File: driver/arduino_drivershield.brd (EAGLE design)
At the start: 60 x 53.7 mm, 37 parts, among them IC1 LB1973M, IC10 LB1973M, IC11 LB1973M, IC12 74HC14D, IC2 LB1973M, IC3 74HC14D, IC4 LB1973M, IC5 LB1973M, IC6 74HC14D, IC7 LB1973M, IC8 LB1973M, IC9 74HC14D, U1 ARDUINO_SHIELDLABEL

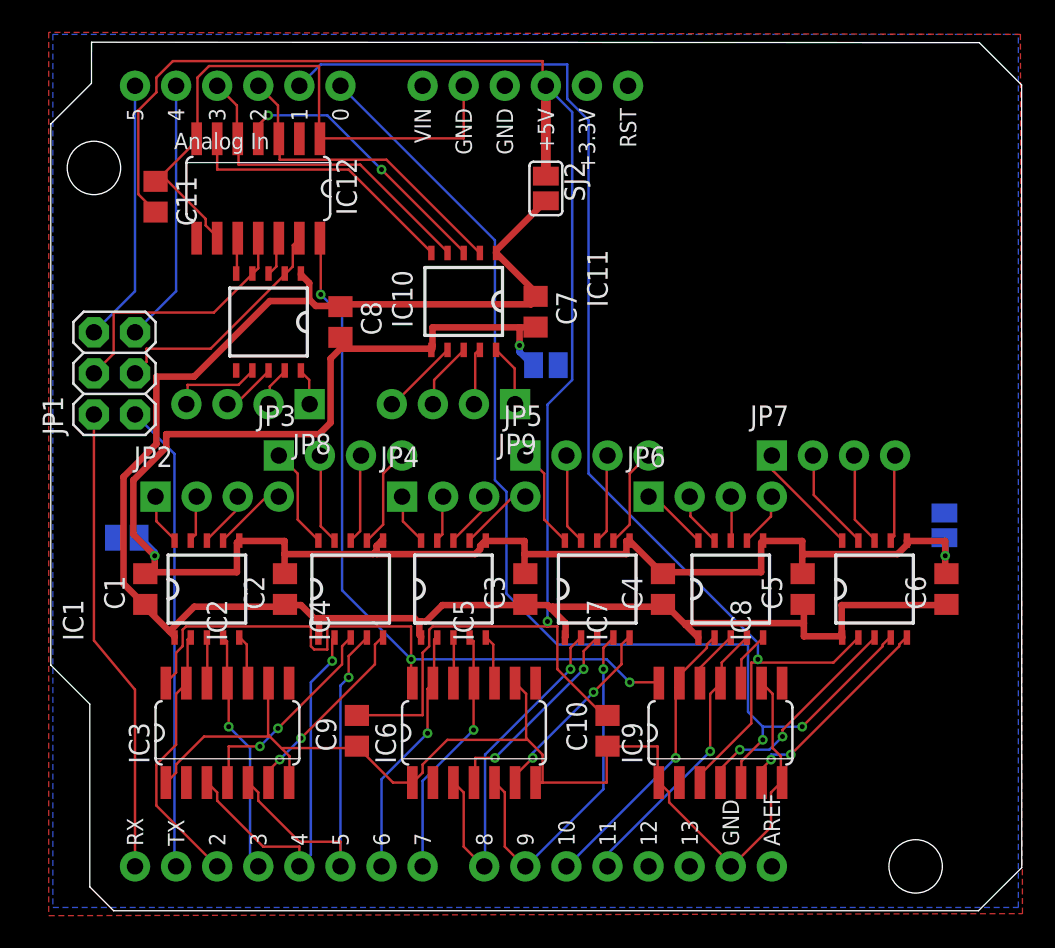
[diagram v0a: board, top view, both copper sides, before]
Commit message: crap, there was still a leftover from myh signal namig adventures
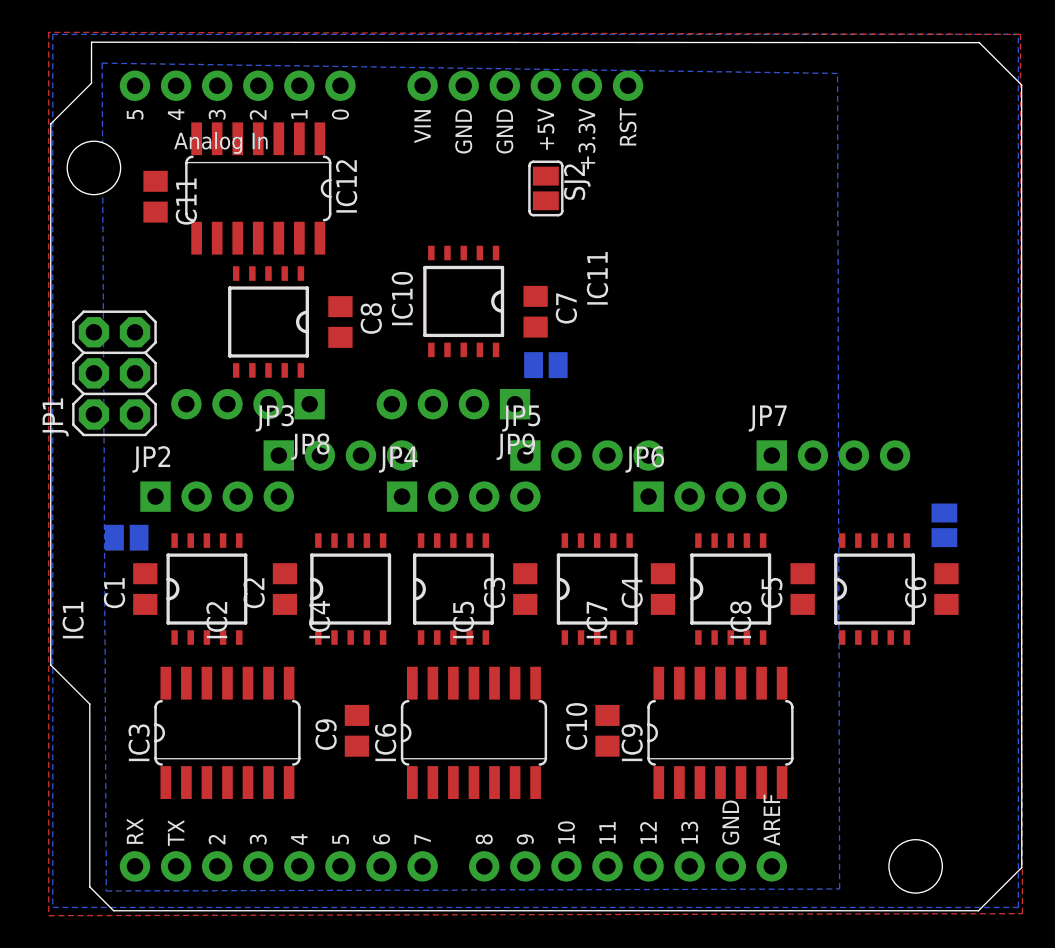
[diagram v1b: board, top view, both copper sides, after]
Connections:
- removed net 5V@1: IC12.14, IC3.14, IC6.14, IC9.14
- net 5V: now also IC12.14, IC3.14, IC6.14, IC9.14
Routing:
- net V+: track 114.7 -> 0.00 mm
- net FOO: track 110.5 -> 0.00 mm, vias 3 -> 0
- net GND: track 109.3 -> 0.00 mm
- net 5V: track 99.9 -> 0.00 mm, vias 1 -> 0
- net N$28: track 75.0 -> 0.00 mm, vias 1 -> 0
- net N$51: track 71.6 -> 0.00 mm, vias 2 -> 0
- net 5V@1: track 68.4 -> 0.00 mm, vias 3 -> 0
- net TX: track 29.0 -> 0.00 mm
- net RX: track 28.9 -> 0.00 mm
- net N$15: track 23.9 -> 0.00 mm, vias 1 -> 0
- net N$16: track 23.9 -> 0.00 mm, vias 1 -> 0
- net N$35: track 22.7 -> 0.00 mm, vias 1 -> 0
- net N$36: track 22.4 -> 0.00 mm, vias 1 -> 0
- net N$66: track 20.6 -> 0.00 mm
- net N$30: track 19.9 -> 0.00 mm
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- added copper zone on layer 16, net N$31

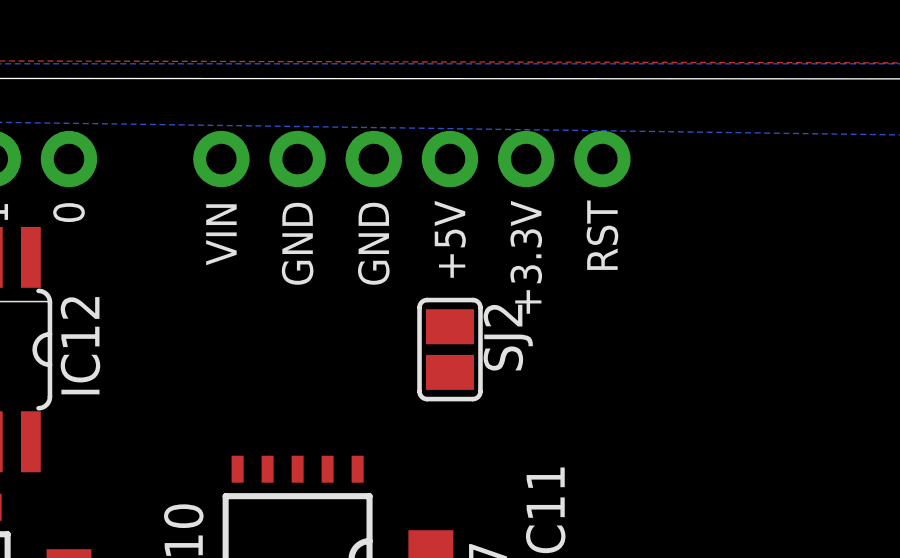
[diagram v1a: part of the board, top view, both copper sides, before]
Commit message: maybe now all my old follies are fixed?
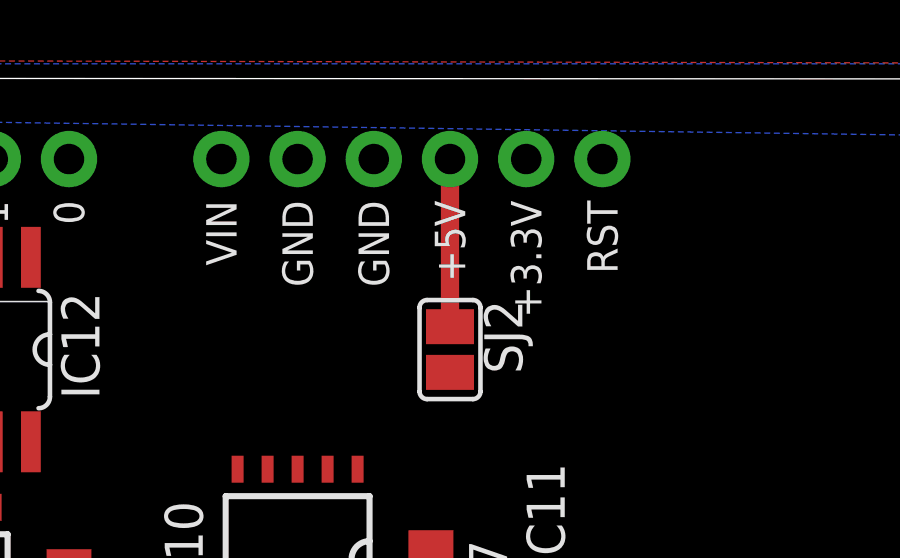
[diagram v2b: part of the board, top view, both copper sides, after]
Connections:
- net FOO: no longer SJ1.1
- net GND@PWR: now also SJ1.1
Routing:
- net 5V: track 0.00 -> 5.59 mm
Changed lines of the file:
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@@
 <contactref element="IC11" pad="6"/>
 <contactref element="IC11" pad="6"/>
-<contactref element="SJ1" pad="1"/>
 <contactref element="SJ3" pad="1"/>
 <contactref element="SJ4" pad="1"/>
@@
 <wire x1="5.715" y1="20.635" x2="11.525" y2="22.681" width="0" layer="19" extent="1-1"/>
 <wire x1="5.334" y1="22.86" x2="5.715" y2="20.635" width="0" layer="19" extent="1-16"/>
-<wire x1="29.718" y1="33.528" x2="26.765" y2="22.681" width="0" layer="19" extent="1-16"/>
-<wire x1="29.845" y1="35.88" x2="29.718" y2="33.528" width="0" layer="19" extent="1-16"/>
-<wire x1="23.4" y1="34.469" x2="29.718" y2="33.528" width="0" layer="19" extent="1-16"/>
+<wire x1="23.4" y1="34.469" x2="20.415" y2="22.681" width="0" layer="19" extent="1-1"/>
 <wire x1="17.78" y1="35.245" x2="23.4" y2="34.469" width="0" layer="19" extent="1-1"/>
+<wire x1="29.845" y1="35.88" x2="23.4" y2="34.469" width="0" layer="19" extent="1-1"/>
 </signal>
 <signal name="GND">
@@
 <contactref element="IC9" pad="14"/>
 <contactref element="IC12" pad="14"/>
-<wire x1="30.48" y1="45.212" x2="30.48" y2="50.8" width="0" layer="19" extent="1-1"/>
+<wire x1="30.48" y1="45.212" x2="30.48" y2="50.8" width="0.6096" layer="1"/>
 <wire x1="16.51" y1="41.3766" x2="30.48" y2="45.212" width="0" layer="19" extent="1-1"/>
 <wire x1="6.35" y1="42.992" x2="16.51" y2="41.3766" width="0" layer="19" extent="1-1"/>
@@
 <signal name="GND@PWR" class="1">
 <contactref element="IC10" pad="6"/>
+<contactref element="SJ1" pad="1"/>
+<wire x1="11.335" y1="33.199" x2="29.718" y2="33.528" width="0" layer="19" extent="1-16"/>
 </signal>
 <signal name="N$31">

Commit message: maybe now all my old follies are fixed?
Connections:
- removed net FOO: C1.2, C2.2, C3.2, C4.2, C5.2, C6.2, C7.2, C8.2, IC1.6, IC11.6, IC2.6, IC4.6, IC5.6, IC7.6, IC8.6, SJ3.1, SJ4.1
- net GND@PWR: now also C1.2, C2.2, C3.2, C4.2, C5.2, C6.2, C7.2, C8.2, IC1.6, IC11.6, IC2.6, IC4.6, IC5.6, IC7.6, IC8.6, SJ3.1, SJ4.1
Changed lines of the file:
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@@
 <wire x1="5.715" y1="18.735" x2="7.525" y2="16.689" width="0" layer="19" extent="1-1"/>
-</signal>
-<signal name="FOO" class="1">
-<contactref element="IC8" pad="6"/>
-<contactref element="IC7" pad="6"/>
-<contactref element="IC5" pad="6"/>
-<contactref element="IC4" pad="6"/>
-<contactref element="IC2" pad="6"/>
-<contactref element="IC1" pad="6"/>
-<contactref element="C8" pad="2"/>
-<contactref element="C7" pad="2"/>
-<contactref element="C6" pad="2"/>
-<contactref element="C5" pad="2"/>
-<contactref element="C4" pad="2"/>
-<contactref element="C3" pad="2"/>
-<contactref element="C2" pad="2"/>
-<contactref element="C1" pad="2"/>
-<contactref element="IC11" pad="6"/>
-<contactref element="IC11" pad="6"/>
-<contactref element="SJ3" pad="1"/>
-<contactref element="SJ4" pad="1"/>
-<wire x1="55.245" y1="20.635" x2="55.118" y2="22.86" width="0" layer="19" extent="1-16"/>
-<wire x1="52.8" y1="22.681" x2="55.118" y2="22.86" width="0" layer="19" extent="1-16"/>
-<wire x1="46.355" y1="20.635" x2="52.8" y2="22.681" width="0" layer="19" extent="1-1"/>
-<wire x1="43.91" y1="22.681" x2="46.355" y2="20.635" width="0" layer="19" extent="1-1"/>
-<wire x1="37.719" y1="20.635" x2="43.91" y2="22.681" width="0" layer="19" extent="1-1"/>
-<wire x1="35.655" y1="22.681" x2="37.719" y2="20.635" width="0" layer="19" extent="1-1"/>
-<wire x1="29.21" y1="20.635" x2="35.655" y2="22.681" width="0" layer="19" extent="1-1"/>
-<wire x1="26.765" y1="22.681" x2="29.21" y2="20.635" width="0" layer="19" extent="1-1"/>
-<wire x1="20.415" y1="22.681" x2="26.765" y2="22.681" width="0" layer="19" extent="1-1"/>
-<wire x1="14.351" y1="20.635" x2="20.415" y2="22.681" width="0" layer="19" extent="1-1"/>
-<wire x1="11.525" y1="22.681" x2="14.351" y2="20.635" width="0" layer="19" extent="1-1"/>
-<wire x1="5.715" y1="20.635" x2="11.525" y2="22.681" width="0" layer="19" extent="1-1"/>
-<wire x1="5.334" y1="22.86" x2="5.715" y2="20.635" width="0" layer="19" extent="1-16"/>
-<wire x1="23.4" y1="34.469" x2="20.415" y2="22.681" width="0" layer="19" extent="1-1"/>
-<wire x1="17.78" y1="35.245" x2="23.4" y2="34.469" width="0" layer="19" extent="1-1"/>
-<wire x1="29.845" y1="35.88" x2="23.4" y2="34.469" width="0" layer="19" extent="1-1"/>
 </signal>
 <signal name="GND">
@@
 <contactref element="IC10" pad="6"/>
 <contactref element="SJ1" pad="1"/>
-<wire x1="11.335" y1="33.199" x2="29.718" y2="33.528" width="0" layer="19" extent="1-16"/>
+<contactref element="IC8" pad="6"/>
+<contactref element="IC7" pad="6"/>
+<contactref element="IC5" pad="6"/>
+<contactref element="IC4" pad="6"/>
+<contactref element="IC2" pad="6"/>
+<contactref element="IC1" pad="6"/>
+<contactref element="C8" pad="2"/>
+<contactref element="C7" pad="2"/>
+<contactref element="C6" pad="2"/>
+<contactref element="C5" pad="2"/>
+<contactref element="C4" pad="2"/>
+<contactref element="C3" pad="2"/>
+<contactref element="C2" pad="2"/>
+<contactref element="C1" pad="2"/>
+<contactref element="IC11" pad="6"/>
+<contactref element="IC11" pad="6"/>
+<contactref element="SJ3" pad="1"/>
+<contactref element="SJ4" pad="1"/>
+<wire x1="55.245" y1="20.635" x2="55.118" y2="22.86" width="0" layer="19" extent="1-16"/>
+<wire x1="52.8" y1="22.681" x2="55.118" y2="22.86" width="0" layer="19" extent="1-16"/>
+<wire x1="46.355" y1="20.635" x2="52.8" y2="22.681" width="0" layer="19" extent="1-1"/>
+<wire x1="43.91" y1="22.681" x2="46.355" y2="20.635" width="0" layer="19" extent="1-1"/>
+<wire x1="37.719" y1="20.635" x2="43.91" y2="22.681" width="0" layer="19" extent="1-1"/>
+<wire x1="35.655" y1="22.681" x2="37.719" y2="20.635" width="0" layer="19" extent="1-1"/>
+<wire x1="29.21" y1="20.635" x2="35.655" y2="22.681" width="0" layer="19" extent="1-1"/>
+<wire x1="26.765" y1="22.681" x2="29.21" y2="20.635" width="0" layer="19" extent="1-1"/>
+<wire x1="20.415" y1="22.681" x2="26.765" y2="22.681" width="0" layer="19" extent="1-1"/>
+<wire x1="14.351" y1="20.635" x2="20.415" y2="22.681" width="0" layer="19" extent="1-1"/>
+<wire x1="11.525" y1="22.681" x2="14.351" y2="20.635" width="0" layer="19" extent="1-1"/>
+<wire x1="5.715" y1="20.635" x2="11.525" y2="22.681" width="0" layer="19" extent="1-1"/>
+<wire x1="5.334" y1="22.86" x2="5.715" y2="20.635" width="0" layer="19" extent="1-16"/>
+<wire x1="11.335" y1="33.199" x2="11.525" y2="22.681" width="0" layer="19" extent="1-1"/>
+<wire x1="17.78" y1="35.245" x2="11.335" y2="33.199" width="0" layer="19" extent="1-1"/>
+<wire x1="23.4" y1="34.469" x2="17.78" y2="35.245" width="0" layer="19" extent="1-1"/>
+<wire x1="29.718" y1="33.528" x2="23.4" y2="34.469" width="0" layer="19" extent="1-16"/>
+<wire x1="29.845" y1="35.88" x2="29.718" y2="33.528" width="0" layer="19" extent="1-16"/>
 </signal>
 <signal name="N$31">

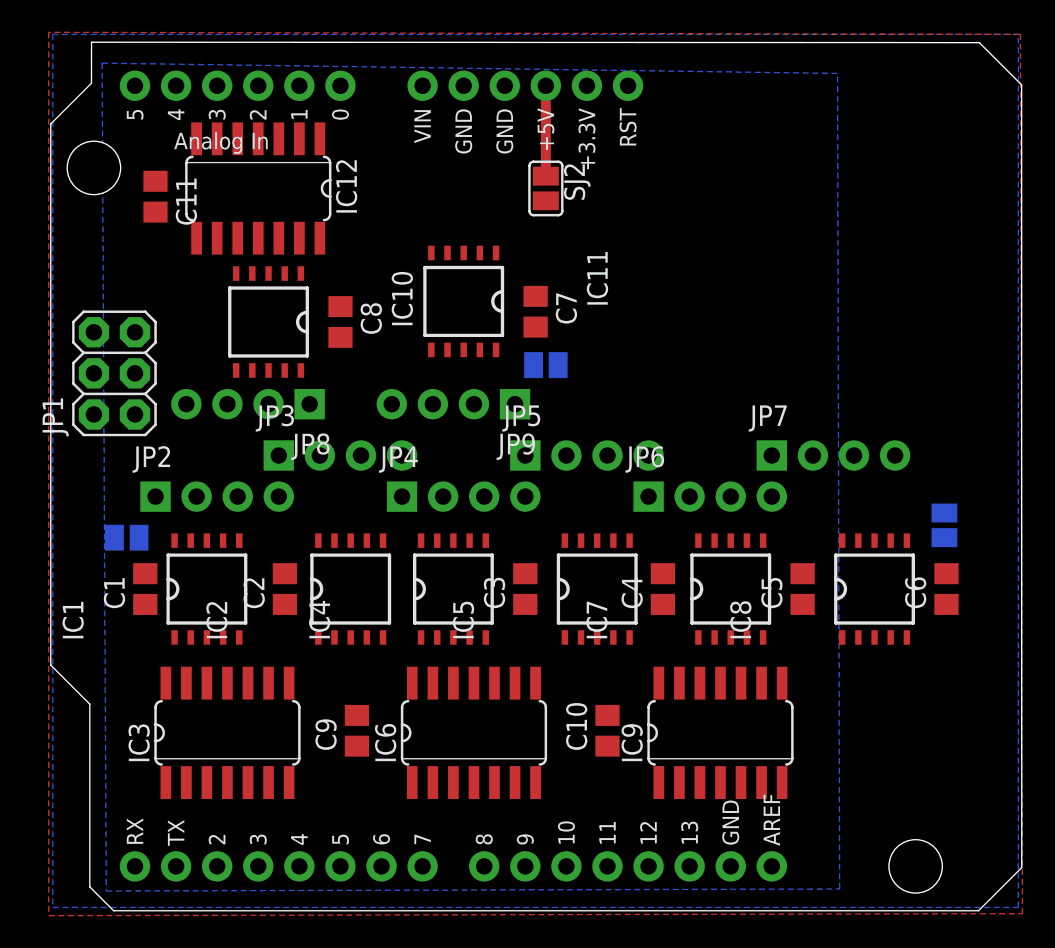
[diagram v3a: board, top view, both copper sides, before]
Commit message: added via to get more ground coverage
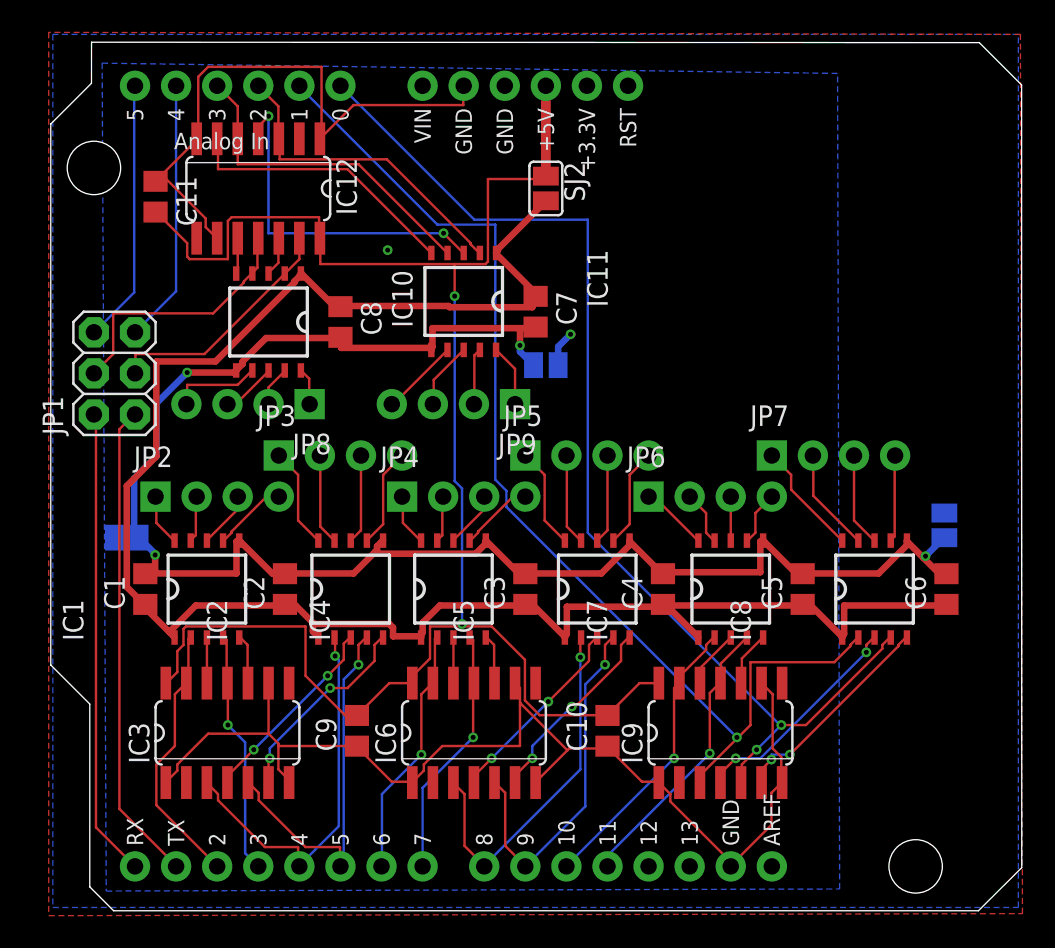
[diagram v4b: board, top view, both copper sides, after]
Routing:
- net V+: track 0.00 -> 115.4 mm
- net GND: track 0.00 -> 108.8 mm, vias 0 -> 2
- net GND@PWR: track 0.00 -> 105.6 mm, vias 0 -> 4
- net 5V: track 5.59 -> 110.2 mm, vias 0 -> 2
- net N$28: track 0.00 -> 69.7 mm, vias 0 -> 1
- net N$51: track 0.00 -> 68.7 mm, vias 0 -> 2
- net TX: track 0.00 -> 29.8 mm
- net RX: track 0.00 -> 29.0 mm
- net N$15: track 0.00 -> 24.0 mm, vias 0 -> 1
- net N$16: track 0.00 -> 23.7 mm, vias 0 -> 1
- net N$35: track 0.00 -> 22.6 mm, vias 0 -> 1
- net N$36: track 0.00 -> 22.4 mm, vias 0 -> 1
- net N$69: track 0.00 -> 21.5 mm, vias 0 -> 2
- net N$66: track 0.00 -> 20.6 mm
- net N$30: track 0.00 -> 19.9 mm
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- removed copper zone on layer 16, net N$31

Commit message: the bottom is now good
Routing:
- net GND: vias 2 -> 7
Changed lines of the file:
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@@
 <grid distance="5" unitdist="mil" unit="mil" style="lines" multiple="1" display="yes" altdistance="0.025" altunitdist="inch" altunit="mil"/>
 <layers>
-<layer number="1" name="Top" color="4" fill="1" visible="no" active="yes"/>
+<layer number="1" name="Top" color="4" fill="1" visible="yes" active="yes"/>
 <layer number="2" name="Route2" color="1" fill="3" visible="no" active="no"/>
 <layer number="3" name="Route3" color="4" fill="3" visible="no" active="no"/>
@@
 <vertex x="48.514" y="51.562"/>
 </polygon>
+<via x="18.415" y="43.053" extent="1-16" drill="0.3048"/>
+<via x="19.685" y="47.625" extent="1-16" drill="0.3048"/>
+<via x="43.815" y="11.176" extent="1-16" drill="0.3048"/>
+<via x="16.51" y="7.62" extent="1-16" drill="0.3048"/>
+<via x="6.35" y="47.244" extent="1-16" drill="0.3048"/>
 </signal>
 <signal name="5V">

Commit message: a few more vias to get more copper under the h-bridges to move heat
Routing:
- net GND: vias 7 -> 12
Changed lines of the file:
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@@
 <via x="16.51" y="7.62" extent="1-16" drill="0.3048"/>
 <via x="6.35" y="47.244" extent="1-16" drill="0.3048"/>
+<via x="21.463" y="19.431" extent="1-16" drill="0.3048"/>
+<via x="30.861" y="19.431" extent="1-16" drill="0.3048"/>
+<via x="39.497" y="19.685" extent="1-16" drill="0.3048"/>
+<via x="47.879" y="19.431" extent="1-16" drill="0.3048"/>
+<via x="9.906" y="19.685" extent="1-16" drill="0.3048"/>
 </signal>
 <signal name="5V">

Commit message: routed the v+ around as well so the "far side" ICs have shorter current path as well
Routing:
- net V+: track 115.4 -> 161.8 mm
- net GND: vias 12 -> 13
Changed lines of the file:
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@@
 <wire x1="27.432" y1="40.386" x2="27.4" y2="40.461" width="0.4064" layer="1"/>
 <wire x1="29.7942" y1="37.7952" x2="29.845" y2="37.78" width="0.4064" layer="1"/>
-<wire x1="27.5082" y1="40.6908" x2="30.48" y2="43.6626" width="0.4064" layer="1"/>
 <wire x1="27.5082" y1="40.6146" x2="27.5082" y2="40.6908" width="0.4064" layer="1"/>
 <wire x1="30.48" y1="43.6626" x2="30.48" y2="43.688" width="0.4064" layer="1"/>
@@
 <wire x1="15.24" y1="39.0144" x2="15.335" y2="39.191" width="0.4064" layer="1"/>
 <wire x1="5.5626" y1="18.8214" x2="5.715" y2="18.735" width="0.4064" layer="1"/>
+<wire x1="30.48" y1="43.6626" x2="41.6814" y2="43.6626" width="0.4064" layer="1"/>
+<wire x1="41.6814" y1="43.6626" x2="58.293" y2="27.051" width="0.4064" layer="1"/>
+<wire x1="58.293" y1="27.051" x2="58.293" y2="20.64" width="0.4064" layer="1"/>
+<wire x1="58.293" y1="20.64" x2="55.245" y2="18.735" width="0.4064" layer="1"/>
+<wire x1="30.353" y1="43.561" x2="30.353" y2="37.719" width="0.4064" layer="1"/>
+<wire x1="30.48" y1="43.6626" x2="30.353" y2="43.561" width="0" layer="19" extent="1-1"/>
 </signal>
 <signal name="GND">
@@
 <via x="47.879" y="19.431" extent="1-16" drill="0.3048"/>
 <via x="9.906" y="19.685" extent="1-16" drill="0.3048"/>
+<via x="37.084" y="38.989" extent="1-16" drill="0.3048"/>
 </signal>
 <signal name="5V">
